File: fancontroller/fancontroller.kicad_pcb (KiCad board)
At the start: 2 copper layers, 96.2 x 53.4 mm, 84 parts, among them J1 Power, J2 Debug, M1 FAN0, M2 FAN0, M3 FAN0, M4 FAN0, M5 FAN0, M6 FAN0, P1 USB_C_Plug_USB2.0, Q1 SS8050-G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

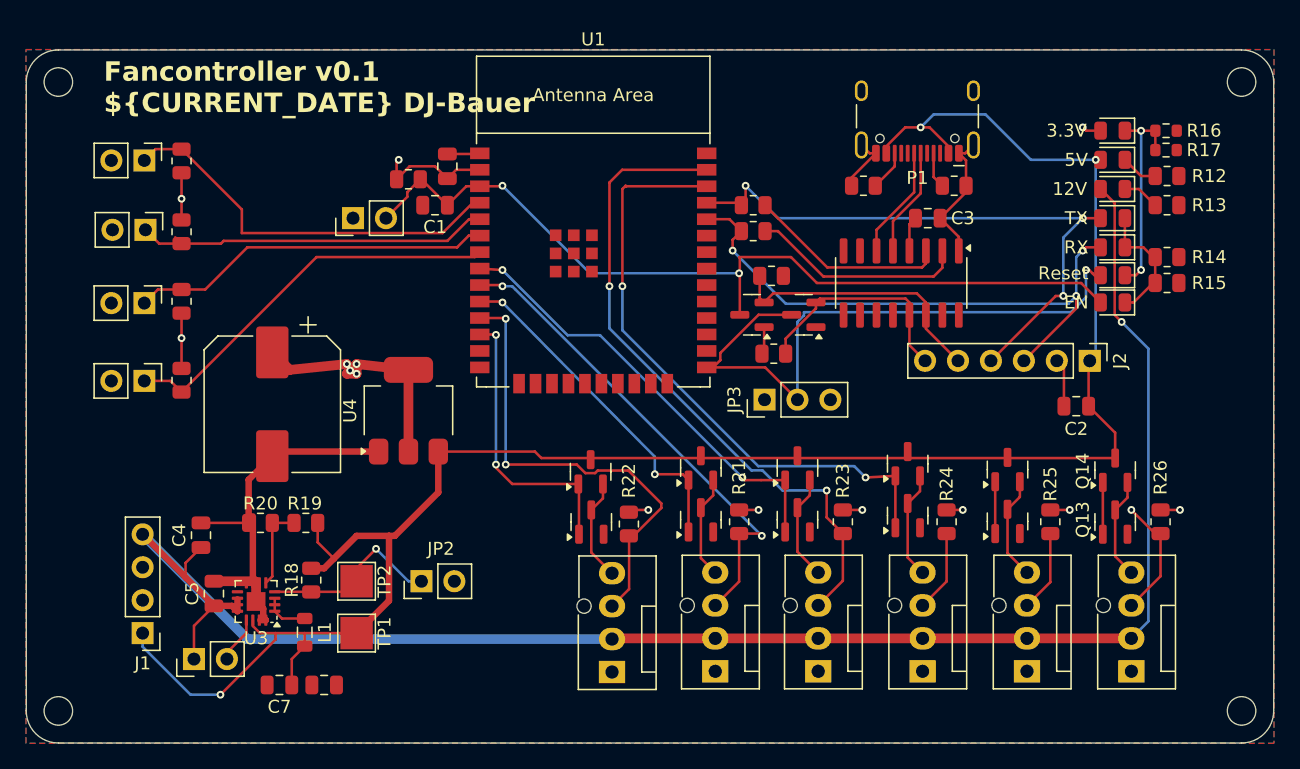
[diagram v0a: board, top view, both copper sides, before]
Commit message: Add i2c ADC
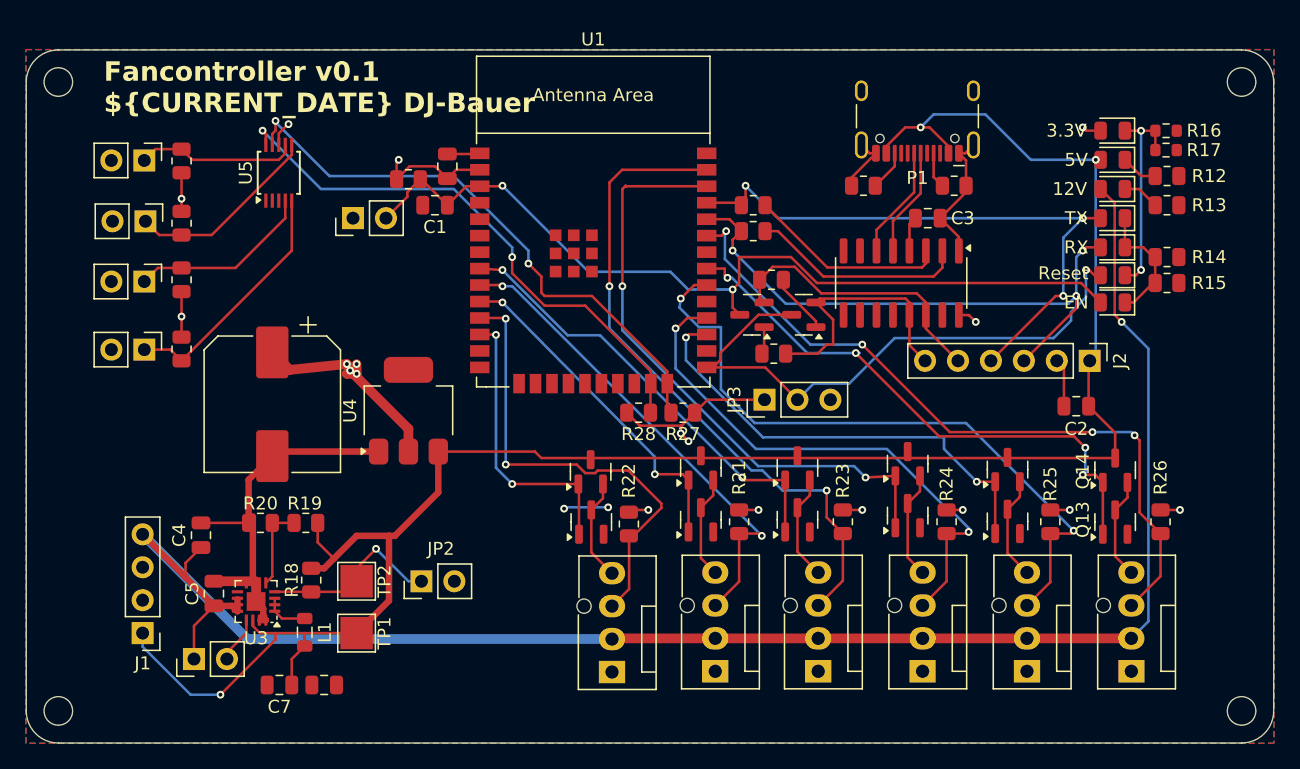
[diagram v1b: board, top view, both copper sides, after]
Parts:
- added GNU: Symbol_GNU-Logo_SilkscreenTop, Symbol:Symbol_GNU-Logo_SilkscreenTop, B.Cu at (72.5, 99.1)
- added R27: 10k, Resistor_SMD:R_0805_2012Metric, F.Cu at (79.2, 114.5)
- added R28: 10k, Resistor_SMD:R_0805_2012Metric, F.Cu at (75.8, 114.5)
- added REF**: OSHW-Symbol_13.4x12mm_SilkScreen, Symbol:OSHW-Symbol_13.4x12mm_SilkScreen, B.Cu at (113.3, 98.3)
- added U5: ADS1115IDGS, Package_SO:TSSOP-10_3x3mm_P0.5mm, F.Cu at (48.0, 96.0)
- SW1: value Reset -> RESET
- moved R2 2.41 mm to (40.5, 109.6)
- moved TH1 2.41 mm to (37.6, 109.6)
- moved R3 1.66 mm to (40.5, 104.2)
- moved TH2 1.66 mm to (37.6, 104.4)
- moved TH3 0.66 mm to (37.7, 99.7)
- moved R4 0.66 mm to (40.5, 99.9)
- moved R9 0.30 mm to (86.0, 104.2)
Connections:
- U1 pad 23: unconnected-(U1-IO15-Pad23) -> SCL
- U1 pad 24: unconnected-(U1-IO2-Pad24) -> SDA
- U1 pad 27: /PWM 5 -> /PWM 4
- U1 pad 28: /Tacho 5 -> /Tacho 3
- U1 pad 30: /Tacho 3 -> /Tacho 4
- U1 pad 31: /PWM 4 -> /PWM 5
- U1 pad 33: /Tacho 4 -> /Tacho 5
- U1 pad 4: TMP3 -> unconnected-(U1-IO36-Pad4)
- U1 pad 5: TMP2 -> unconnected-(U1-IO39-Pad5)
- U1 pad 6: TMP1 -> unconnected-(U1-IO34-Pad6)
- U1 pad 7: TMP0 -> unconnected-(U1-IO35-Pad7)
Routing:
- net /Tacho 5: track 9.48 -> 55.9 mm, vias 1 -> 4
- net /Tacho 4: track 6.29 -> 51.8 mm, vias 0 -> 2
- net SDA: track 0.00 -> 44.8 mm, vias 0 -> 2
- net SCL: track 0.00 -> 43.2 mm, vias 0 -> 2
- net /PWM 5: track 4.00 -> 43.8 mm, vias 0 -> 4
- net /Tacho 3: track 6.31 -> 42.0 mm, vias 0 -> 2
- net /PWM 4: track 4.00 -> 35.4 mm, vias 0 -> 2
- net TMP3: track 31.3 -> 12.4 mm
- net TMP2: track 29.1 -> 15.1 mm
- net TMP1: track 28.0 -> 14.2 mm
- net +3.3V: track 47.3 -> 59.7 mm, vias 14 -> 18
- net TMP0: track 30.7 -> 19.1 mm
- net Net-(Q2-B): track 0.00 -> 4.69 mm
- net GND: track 51.5 -> 55.0 mm, vias 0 -> 2
- net RST: track 49.2 -> 45.9 mm
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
